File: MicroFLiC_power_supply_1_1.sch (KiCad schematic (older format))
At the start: 17 parts, among them P1 BARREL_JACK, P2 CONN_02X03, P3 Socket_1x14, P4 Socket_2x2, SW1 SW_PUSH_RA

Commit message: Added load resistor. Changed part references in consequence.
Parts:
- P3: Part Number ESQ-114-33-G-S -> ESQ-114-33-G-S
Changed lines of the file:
@@
 F 2 "jakub:ESQ-114-33-S-G" H 7300 4050 60  0001 C CNN
 F 3 "" H 7300 4050 60  0000 C CNN
-F 4 " ESQ-114-33-G-S" H 7300 4050 60  0001 C CNN "Part Number"
+F 4 "ESQ-114-33-G-S" H 7300 4050 60  0001 C CNN "Part Number"
 F 5 "Samtec" H 7300 4050 60  0001 C CNN "Manufacturer"
 F 6 "1930609" H 7300 4050 60  0001 C CNN "Order Code"

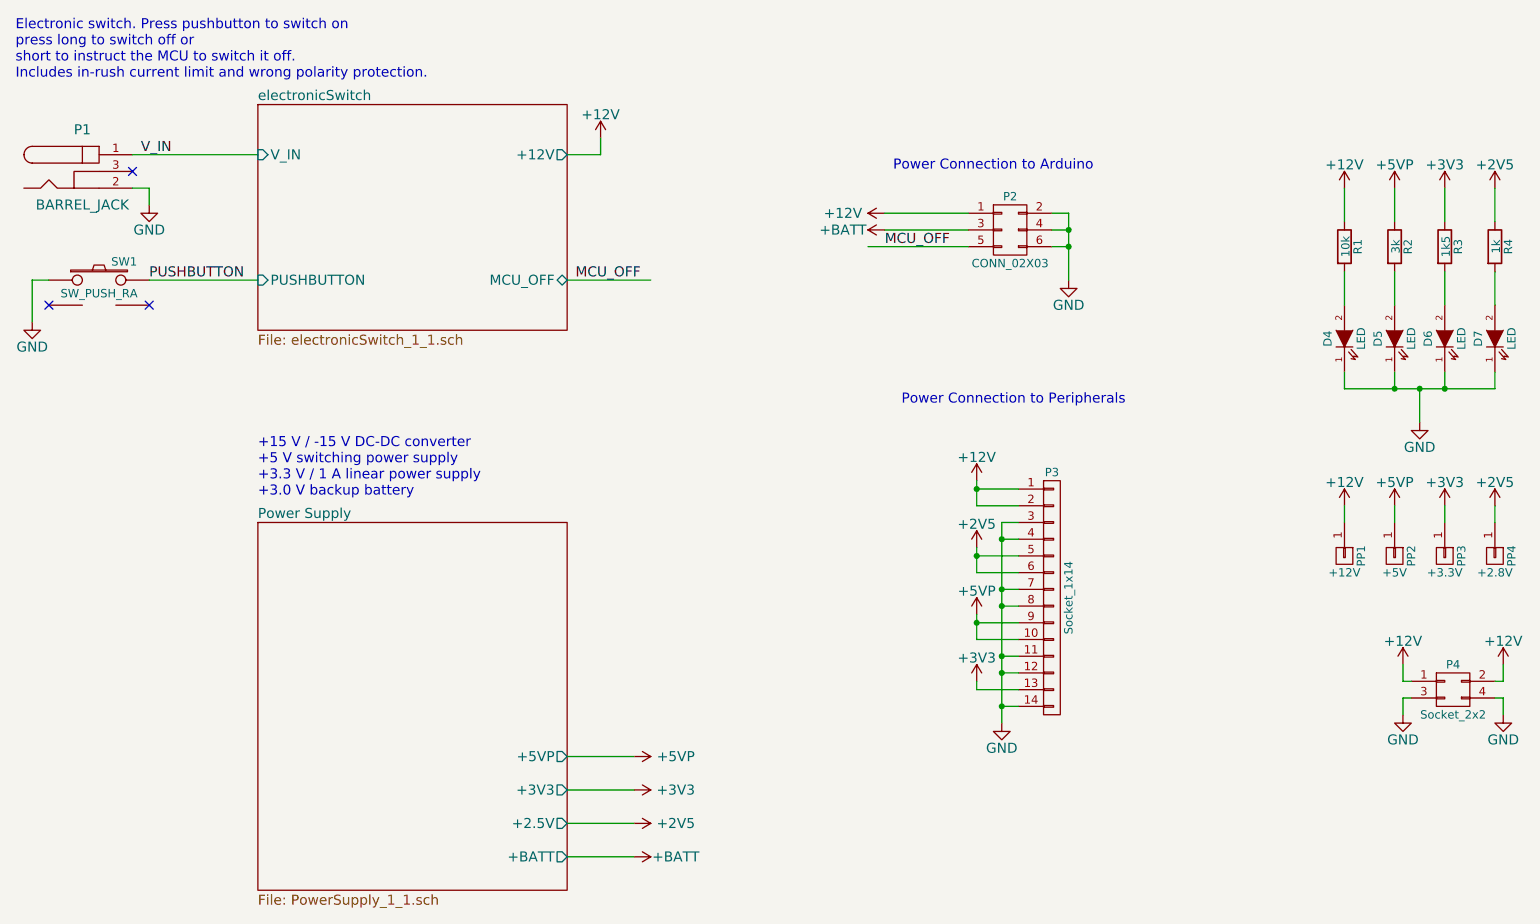
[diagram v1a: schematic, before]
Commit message: Added detailed part descriptions
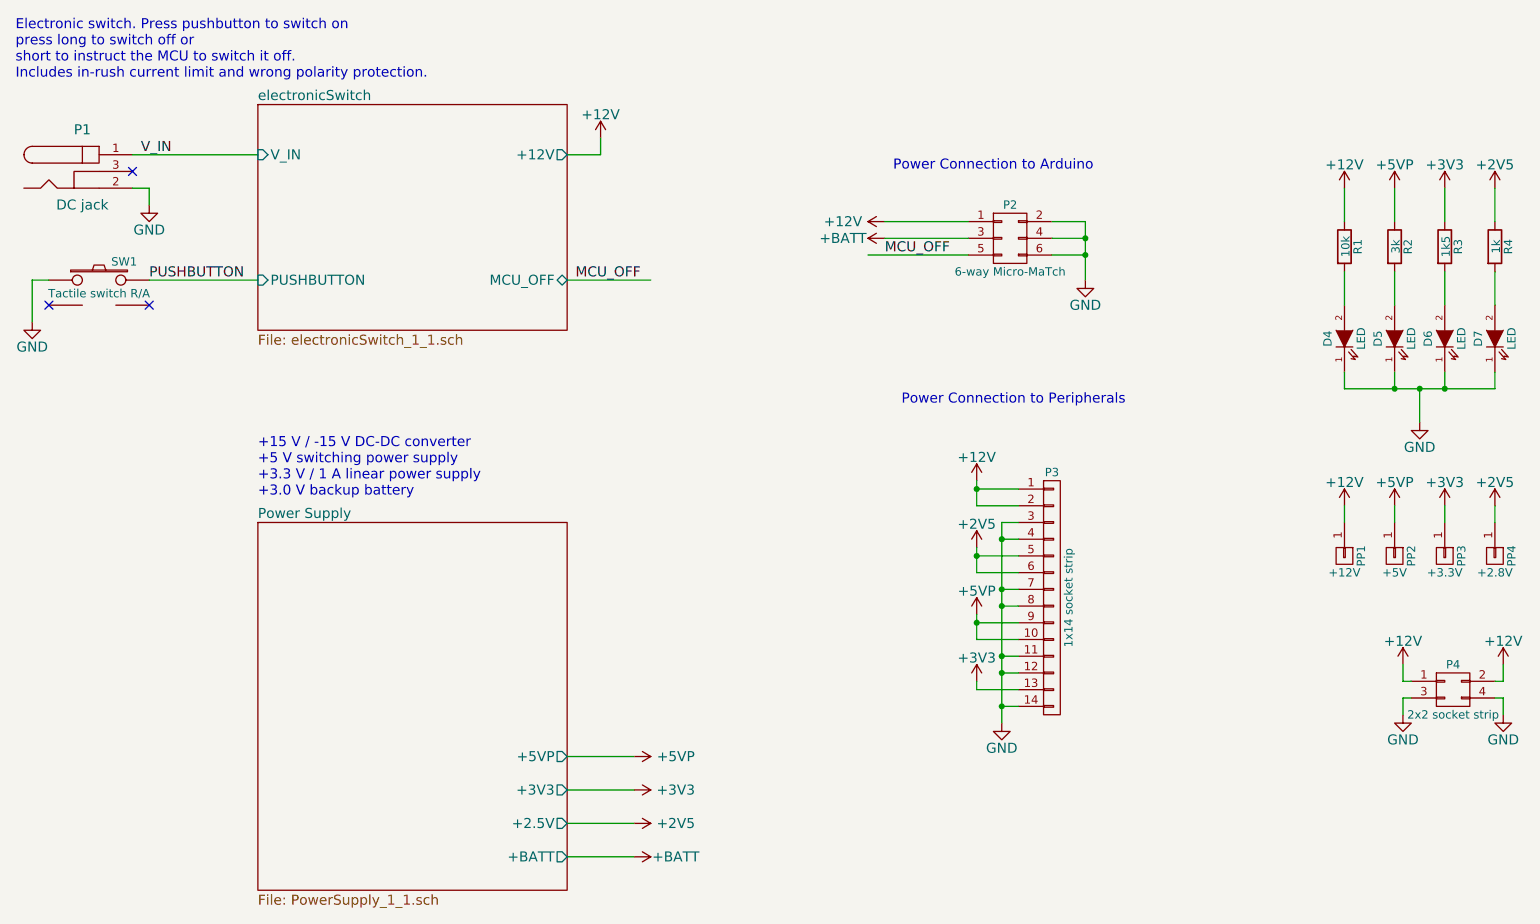
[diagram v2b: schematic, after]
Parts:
- D4, D5, D6, D7: Alt. Order Code (none) -> 630-HSMY-C150; Alt. Supplier (none) -> Mouser; Note (none) -> Yellow 1206 LED; Order Code 8554773 -> 2497382; Package (none) -> 1206; Supplier (none) -> Farnell
- P1: value BARREL_JACK -> DC jack; Alt. Order Code (none) -> 502-RAPC722X; Alt. Supplier (none) -> Mouser; Note (none) -> 2.1/2.5mm DC jack R/A; Package (none) -> DC jack R/A; Supplier (none) -> Farnell
- P2: value CONN_02X03 -> 6-way Micro-MaTch; Alt. Order Code (none) -> 571-71882756; Alt. Supplier (none) -> Mouser; Note (none) -> 6-way SMD Micro-MaTch connector; Package (none) -> Micro-MaTch SMD; Supplier (none) -> Farnell
- P3: value Socket_1x14 -> 1x14 socket strip; Alt. Order Code (none) -> ESQ-114-33-G-S; Alt. Supplier (none) -> Samtec; Note (none) -> 1x14 ESQ series elevated socket strip; Package (none) -> SIL-14; Supplier (none) -> Farnell
- P4: value Socket_2x2 -> 2x2 socket strip; Alt. Order Code (none) -> ESQ-102-33-G-D; Alt. Supplier (none) -> Samtec; Note (none) -> 2x2 ESQ series elevated socket strip; Package (none) -> DIL-4; Supplier (none) -> Farnell
- R1: Alt. Order Code (none) -> 71-CRCW0805-10K-E3; Alt. Supplier (none) -> Mouser; Note (none) -> 10kΩ/1% 0805 resistor; Package (none) -> 0805; Supplier (none) -> Farnell
- R2: Alt. Order Code (none) -> 667-ERJ-6GEYJ302V; Alt. Supplier (none) -> Mouser; Note (none) -> 3kΩ/1% 0805 resistor; Package (none) -> 0805; Supplier (none) -> Farnell
- R3: Alt. Order Code (none) -> 71-CRCW0805-1.5K-E3; Alt. Supplier (none) -> Mouser; Note (none) -> 1.5kΩ/1% 0805 resistor; Package (none) -> 0805; Supplier (none) -> Farnell
- R4: Alt. Order Code (none) -> 71-CRCW0805-1.0K-E3; Alt. Supplier (none) -> Mouser; Note (none) -> 1kΩ/1% 0805 resistor; Package (none) -> 0805; Supplier (none) -> Farnell
- SW1: value SW_PUSH_RA -> Tactile switch R/A; Alt. Order Code (none) -> 506-FSMRA3JH; Alt. Supplier (none) -> Mouser; Note (none) -> Right-angle tactile switch; Package (none) -> R/A pushbutton; Supplier (none) -> Farnell
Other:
- moved on the sheet: P2
